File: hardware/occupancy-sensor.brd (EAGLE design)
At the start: 25.5 x 7 mm, 8 parts, among them U1 QRE1113, U2 QRE1113

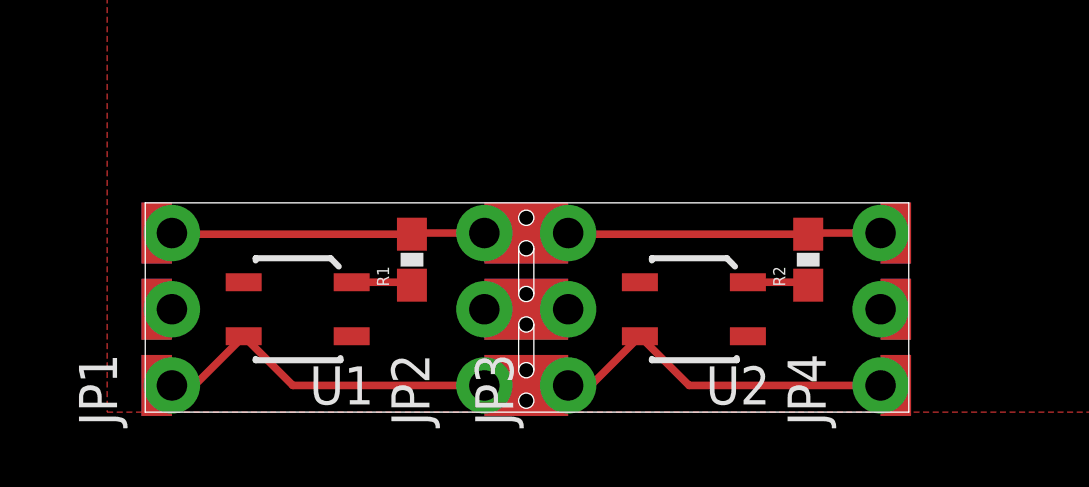
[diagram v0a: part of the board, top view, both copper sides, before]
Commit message: occupancy sensor improvements
* rounded corners
* labels
* larger pads
* more perforations
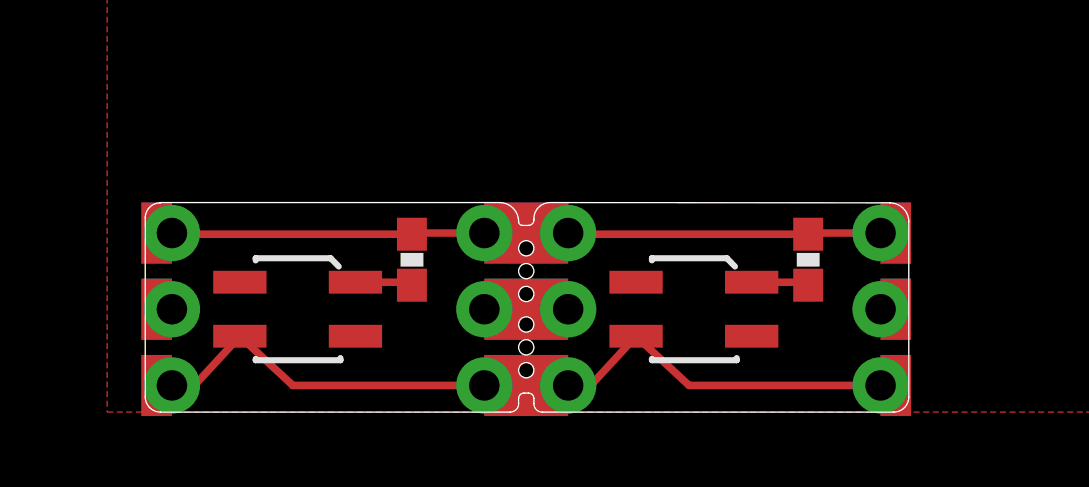
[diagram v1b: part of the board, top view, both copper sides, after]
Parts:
- U1, U2: device SparkFun-Sensors:QRE1113 -> SparkFun-Sensors:QRE1113-W
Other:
- outline, holes or cut-outs redrawn
- board text added: "5V"
- board text added: "GND"
- board text added: "SIG"
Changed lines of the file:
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@@
 <board>
 <plain>
-<wire x1="0" y1="0" x2="25.451" y2="0" width="0" layer="20"/>
-<wire x1="25.451" y1="0" x2="25.451" y2="6.975" width="0" layer="20"/>
-<wire x1="25.451" y1="6.975" x2="0" y2="6.975" width="0" layer="20"/>
-<wire x1="0" y1="6.975" x2="0" y2="0" width="0" layer="20"/>
+<wire x1="0" y1="6.477" x2="0" y2="0.508" width="0" layer="20"/>
+<wire x1="0" y1="0.508" x2="0.508" y2="0" width="0" layer="20" curve="90"/>
+<wire x1="0.508" y1="0" x2="12.162021875" y2="0" width="0" layer="20"/>
+<wire x1="12.162021875" y1="0" x2="12.446" y2="0.283978125" width="0" layer="20" curve="90"/>
+<wire x1="12.446" y1="0.283978125" x2="12.446" y2="0.455396875" width="0" layer="20"/>
+<wire x1="12.446" y1="0.455396875" x2="12.625603125" y2="0.635" width="0" layer="20" curve="-90"/>
+<wire x1="12.625603125" y1="0.635" x2="12.774396875" y2="0.635" width="0" layer="20"/>
+<wire x1="12.774396875" y1="0.635" x2="12.954" y2="0.455396875" width="0" layer="20" curve="-90"/>
+<wire x1="12.954" y1="0.455396875" x2="12.954" y2="0.283978125" width="0" layer="20"/>
+<wire x1="12.954" y1="0.283978125" x2="13.237978125" y2="0" width="0" layer="20" curve="90"/>
+<wire x1="13.237978125" y1="0" x2="24.9498625" y2="0" width="0" layer="20"/>
+<wire x1="24.9498625" y1="0" x2="25.451" y2="0.5011375" width="0" layer="20" curve="90"/>
+<wire x1="25.451" y1="0.5011375" x2="25.451" y2="6.347925" width="0" layer="20"/>
+<wire x1="25.451" y1="6.347925" x2="24.823925" y2="6.975" width="0" layer="20" curve="90"/>
+<wire x1="24.823925" y1="6.975" x2="13.493265625" y2="6.984546875" width="0" layer="20"/>
+<wire x1="13.493265625" y1="6.984546875" x2="12.954" y2="6.445734375" width="0" layer="20" curve="90.149954"/>
+<wire x1="12.954" y1="6.445734375" x2="12.954" y2="6.402603125" width="0" layer="20"/>
+<wire x1="12.954" y1="6.402603125" x2="12.774396875" y2="6.223" width="0" layer="20" curve="-90"/>
+<wire x1="12.774396875" y1="6.223" x2="12.573" y2="6.223" width="0" layer="20"/>
+<wire x1="12.573" y1="6.223" x2="12.446" y2="6.35" width="0" layer="20" curve="-90"/>
+<wire x1="12.446" y1="6.35" x2="11.811" y2="6.985" width="0" layer="20" curve="90"/>
+<wire x1="11.811" y1="6.985" x2="0.498" y2="6.985" width="0" layer="20"/>
+<wire x1="0.498" y1="6.985" x2="0.498" y2="6.975" width="0" layer="20"/>
+<wire x1="0.498" y1="6.975" x2="0" y2="6.477" width="0" layer="20" curve="90"/>
 <polygon width="0" layer="29">
 <vertex x="0.889" y="4.445"/>
@@
 <rectangle x1="-0.127" y1="-0.127" x2="0.889" y2="1.905" layer="30"/>
 <hole x="12.7" y="5.461" drill="0.508"/>
-<hole x="12.7" y="6.477" drill="0.508"/>
 <hole x="12.7" y="3.937" drill="0.508"/>
 <hole x="12.7" y="2.921" drill="0.508"/>
 <hole x="12.7" y="1.397" drill="0.508"/>
-<hole x="12.7" y="0.381" drill="0.508"/>
-<wire x1="12.446" y1="1.397" x2="12.446" y2="2.921" width="0" layer="20"/>
-<wire x1="12.954" y1="2.921" x2="12.954" y2="1.397" width="0" layer="20"/>
-<wire x1="12.446" y1="5.461" x2="12.446" y2="3.937" width="0" layer="20"/>
-<wire x1="12.954" y1="3.937" x2="12.954" y2="5.461" width="0" layer="20"/>
 <rectangle x1="11.303" y1="4.953" x2="14.097" y2="6.985" layer="29"/>
 <rectangle x1="11.303" y1="4.953" x2="14.097" y2="6.985" layer="30"/>
@@
 <rectangle x1="24.511" y1="2.413" x2="25.527" y2="4.445" layer="30"/>
 <rectangle x1="24.511" y1="4.953" x2="25.527" y2="6.985" layer="30"/>
+<hole x="12.7" y="2.159" drill="0.508"/>
+<hole x="12.7" y="4.699" drill="0.508"/>
+<text x="6.985" y="5.334" size="1.27" layer="22" rot="MR0">5V</text>
+<text x="7.62" y="2.794" size="1.27" layer="22" rot="MR0">GND</text>
+<text x="7.366" y="0.254" size="1.27" layer="22" rot="MR0">SIG</text>
+<wire x1="2.286" y1="5.969" x2="4.445" y2="5.969" width="0.4064" layer="22"/>
+<wire x1="9.906" y1="5.969" x2="7.493" y2="5.969" width="0.4064" layer="22"/>
+<wire x1="9.906" y1="3.429" x2="8.128" y2="3.429" width="0.4064" layer="22"/>
+<wire x1="2.286" y1="3.429" x2="3.683" y2="3.429" width="0.4064" layer="22"/>
+<wire x1="2.286" y1="0.889" x2="3.937" y2="0.889" width="0.4064" layer="22"/>
+<wire x1="9.906" y1="0.889" x2="7.874" y2="0.889" width="0.4064" layer="22"/>
+<text x="20.193" y="5.334" size="1.27" layer="22" rot="MR0">5V</text>
+<text x="20.828" y="2.794" size="1.27" layer="22" rot="MR0">GND</text>
+<text x="20.574" y="0.254" size="1.27" layer="22" rot="MR0">SIG</text>
+<wire x1="15.494" y1="5.969" x2="17.653" y2="5.969" width="0.4064" layer="22"/>
+<wire x1="23.114" y1="5.969" x2="20.701" y2="5.969" width="0.4064" layer="22"/>
+<wire x1="23.114" y1="3.429" x2="21.336" y2="3.429" width="0.4064" layer="22"/>
+<wire x1="15.494" y1="3.429" x2="16.891" y2="3.429" width="0.4064" layer="22"/>
+<wire x1="15.494" y1="0.889" x2="17.145" y2="0.889" width="0.4064" layer="22"/>
+<wire x1="23.114" y1="0.889" x2="21.082" y2="0.889" width="0.4064" layer="22"/>
 </plain>
 <attributes>
@@
 </autorouter>
 <elements>
-<element name="JP1" library="SparkFun-Connectors" package="1X03_NO_SILK" value="" x="0.889" y="0.889" rot="R90"/>
-<element name="R1" library="SparkFun-Passives" package="0603-RES" value="100" x="8.89" y="5.08" rot="R90"/>
-<element name="R2" library="SparkFun-Passives" package="0603-RES" value="100" x="22.098" y="5.08" rot="R90"/>
-<element name="U1" library="SparkFun-Sensors" package="QRE1113" value="QRE1113" x="5.08" y="3.429" rot="R180">
-<attribute name="PROD_ID" value="IC-09357" x="5.08" y="3.429" size="1.778" layer="27" rot="R180" display="off"/>
+<element name="JP1" library="SparkFun-Connectors" package="1X03_NO_SILK" value="" x="0.889" y="0.889" smashed="yes" rot="R90">
+<attribute name="VALUE" x="4.064" y="-0.381" size="1.27" layer="27" rot="R90"/>
 </element>
-<element name="U2" library="SparkFun-Sensors" package="QRE1113" value="QRE1113" x="18.288" y="3.429" rot="R180">
-<attribute name="PROD_ID" value="IC-09357" x="18.288" y="3.429" size="1.778" layer="27" rot="R180" display="off"/>
+<element name="R1" library="SparkFun-Passives" package="0603-RES" value="100" x="8.89" y="5.08" smashed="yes" rot="R90"/>
+<element name="R2" library="SparkFun-Passives" package="0603-RES" value="100" x="22.098" y="5.08" smashed="yes" rot="R90"/>
+<element name="U1" library="SparkFun-Sensors" package="QRE1113-W" value="QRE1113" x="5.08" y="3.429" smashed="yes" rot="R180"/>
+<element name="U2" library="SparkFun-Sensors" package="QRE1113-W" value="QRE1113" x="18.288" y="3.429" smashed="yes" rot="R180"/>
+<element name="JP2" library="SparkFun-Connectors" package="1X03_NO_SILK" value="" x="11.303" y="0.889" smashed="yes" rot="R90">
+<attribute name="VALUE" x="14.478" y="-0.381" size="1.27" layer="27" rot="R90"/>
 </element>
-<element name="JP2" library="SparkFun-Connectors" package="1X03_NO_SILK" value="" x="11.303" y="0.889" rot="R90"/>
-<element name="JP3" library="SparkFun-Connectors" package="1X03_NO_SILK" value="" x="14.097" y="0.889" rot="R90"/>
-<element name="JP4" library="SparkFun-Connectors" package="1X03_NO_SILK" value="" x="24.511" y="0.889" rot="R90"/>
+<element name="JP3" library="SparkFun-Connectors" package="1X03_NO_SILK" value="" x="14.097" y="0.889" smashed="yes" rot="R90">
+<attribute name="VALUE" x="17.272" y="-0.381" size="1.27" layer="27" rot="R90"/>
+</element>
+<element name="JP4" library="SparkFun-Connectors" package="1X03_NO_SILK" value="" x="24.511" y="0.889" smashed="yes" rot="R90">
+<attribute name="VALUE" x="27.686" y="-0.381" size="1.27" layer="27" rot="R90"/>
+</element>
 </elements>
 <signals>
@@
 <contactref element="U1" pad="1"/>
 <wire x1="8.89" y1="4.23" x2="8.791" y2="4.329" width="0.254" layer="1"/>
-<wire x1="8.791" y1="4.329" x2="6.88" y2="4.329" width="0.254" layer="1"/>
+<wire x1="8.791" y1="4.329" x2="7.007" y2="4.329" width="0.254" layer="1"/>
 </signal>
 <signal name="N$2">
@@
 <contactref element="U2" pad="1"/>
 <wire x1="22.098" y1="4.23" x2="21.999" y2="4.329" width="0.254" layer="1"/>
-<wire x1="21.999" y1="4.329" x2="20.088" y2="4.329" width="0.254" layer="1"/>
+<wire x1="21.999" y1="4.329" x2="20.215" y2="4.329" width="0.254" layer="1"/>
 </signal>
 <signal name="GND">
@@
 <contactref element="JP4" pad="1"/>
 <wire x1="0.889" y1="0.889" x2="1.64" y2="0.889" width="0.254" layer="1"/>
-<wire x1="1.64" y1="0.889" x2="3.28" y2="2.529" width="0.254" layer="1"/>
-<wire x1="3.28" y1="2.529" x2="4.92" y2="0.889" width="0.254" layer="1"/>
+<wire x1="1.64" y1="0.889" x2="3.153" y2="2.529" width="0.254" layer="1"/>
+<wire x1="3.153" y1="2.529" x2="4.92" y2="0.889" width="0.254" layer="1"/>
 <wire x1="4.92" y1="0.889" x2="11.303" y2="0.889" width="0.254" layer="1"/>
 <wire x1="11.303" y1="0.889" x2="14.097" y2="0.889" width="0.254" layer="1"/>
 <wire x1="14.097" y1="0.889" x2="14.848" y2="0.889" width="0.254" layer="1"/>
-<wire x1="14.848" y1="0.889" x2="16.488" y2="2.529" width="0.254" layer="1"/>
-<wire x1="16.488" y1="2.529" x2="18.128" y2="0.889" width="0.254" layer="1"/>
+<wire x1="14.848" y1="0.889" x2="16.361" y2="2.529" width="0.254" layer="1"/>
+<wire x1="16.361" y1="2.529" x2="18.128" y2="0.889" width="0.254" layer="1"/>
 <wire x1="18.128" y1="0.889" x2="24.511" y2="0.889" width="0.254" layer="1"/>
 </signal>
